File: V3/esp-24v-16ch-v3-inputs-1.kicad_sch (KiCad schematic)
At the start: 100 parts, among them U10 OR-3H4-4, U11 OR-3H4-4, U8 OR-3H4-4, U9 OR-3H4-4

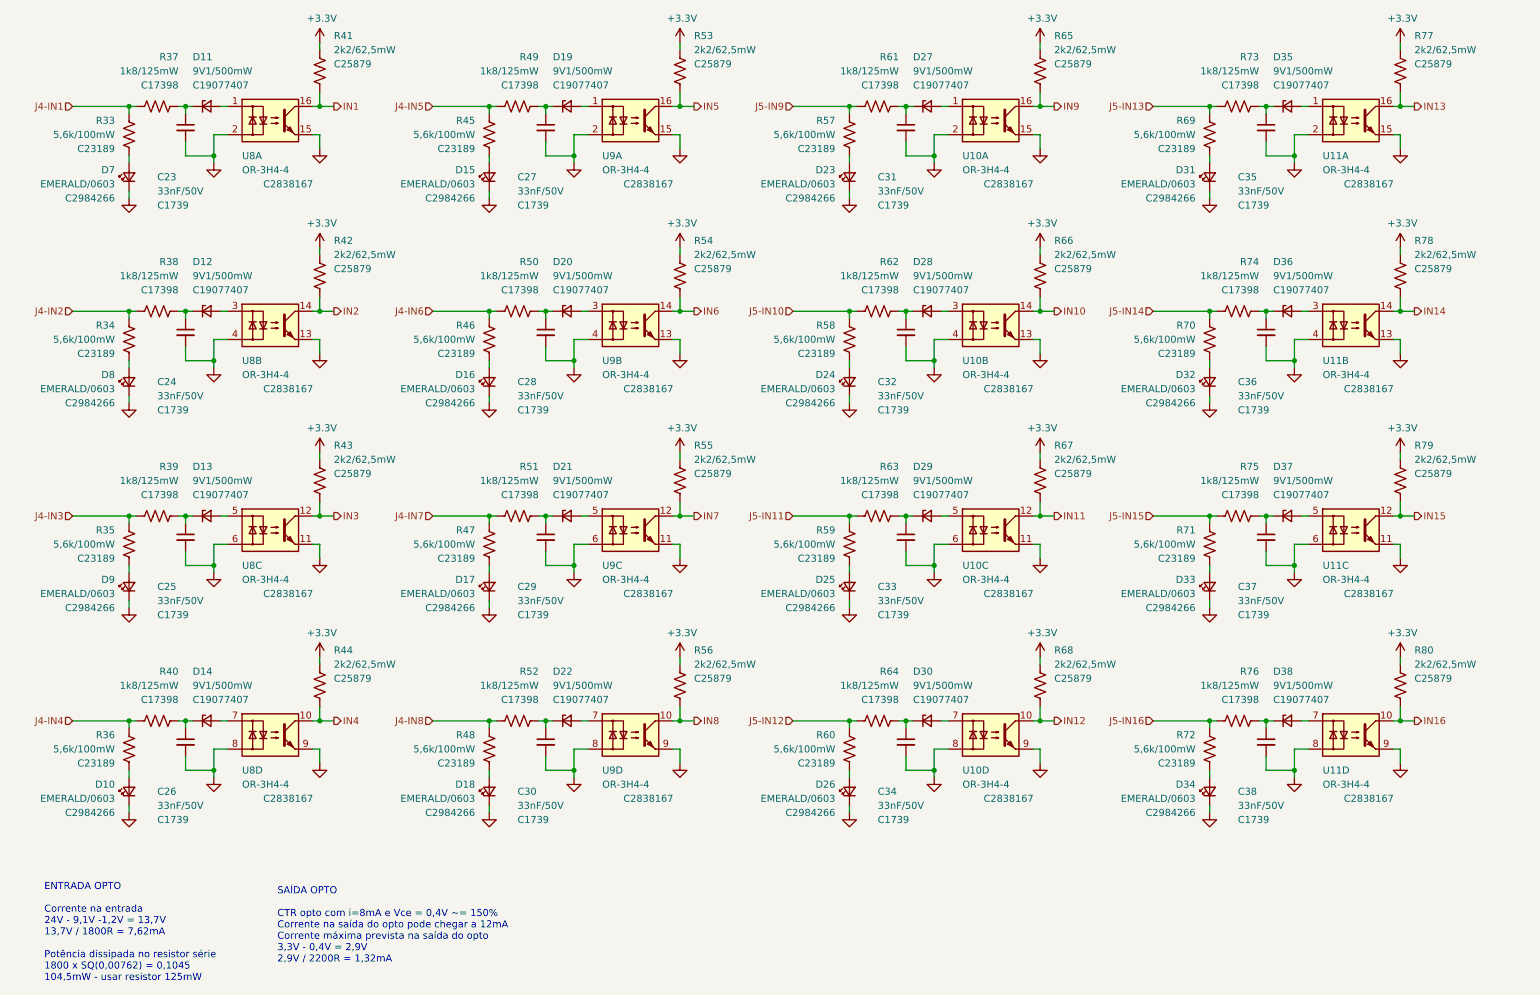
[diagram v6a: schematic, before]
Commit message: Improvements to high speed signals routing
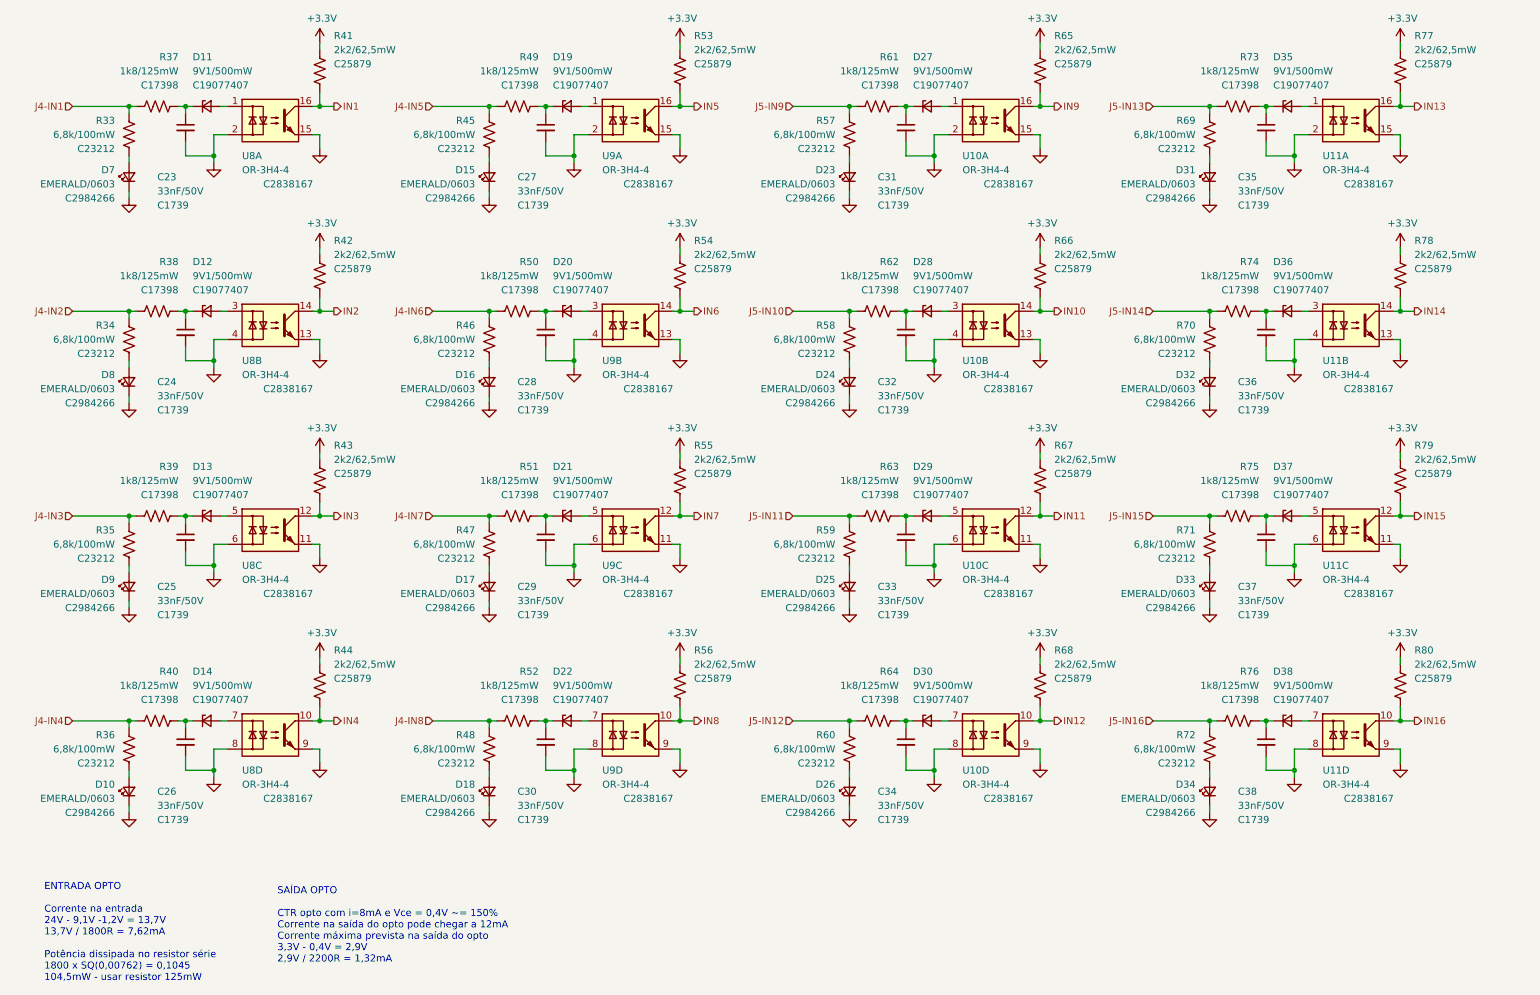
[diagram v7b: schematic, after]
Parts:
- R33, R34, R35, R36, R45, R46, R47, R48, R57, R58, R59, R60, R69, R70, R71, R72: value 5,6k/100mW -> 6,8k/100mW; LCSC Part # C23189 -> C23212; Mfr PN 0603WAF5601T5E -> 0603WAF6801T5E; Vendor PN C23189 -> C23212
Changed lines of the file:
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@@
 			)
 		)
-		(property "Value" "5,6k/100mW"
+		(property "Value" "6,8k/100mW"
 			(at 224.79 76.2 0)
 			(effects
@@
 			)
 		)
-		(property "Mfr PN" "0603WAF5601T5E"
+		(property "Mfr PN" "0603WAF6801T5E"
 			(at 227.33 76.2 0)
 			(effects
@@
 			)
 		)
-		(property "Vendor PN" "C23189"
+		(property "Vendor PN" "C23212 "
 			(at 227.33 76.2 0)
 			(effects
@@
 			)
 		)
-		(property "LCSC Part #" "C23189"
+		(property "LCSC Part #" "C23212"
 			(at 224.79 78.74 0)
 			(effects
@@
 			)
 		)
-		(property "Value" "5,6k/100mW"
+		(property "Value" "6,8k/100mW"
 			(at 95.25 113.03 0)
 			(effects
@@
 			)
 		)
-		(property "Mfr PN" "0603WAF5601T5E"
+		(property "Mfr PN" "0603WAF6801T5E"
 			(at 97.79 113.03 0)
 			(effects
@@
 			)
 		)
-		(property "Vendor PN" "C23189"
+		(property "Vendor PN" "C23212 "
 			(at 97.79 113.03 0)
 			(effects
@@
 			)
 		)
-		(property "LCSC Part #" "C23189"
+		(property "LCSC Part #" "C23212"
 			(at 95.25 115.57 0)
 			(effects
@@
 			)
 		)
-		(property "Value" "5,6k/100mW"
+		(property "Value" "6,8k/100mW"
 			(at 224.79 113.03 0)
 			(effects
@@
 			)
 		)
-		(property "Mfr PN" "0603WAF5601T5E"
+		(property "Mfr PN" "0603WAF6801T5E"
 			(at 227.33 113.03 0)
 			(effects
@@
 			)
 		)
-		(property "Vendor PN" "C23189"
+		(property "Vendor PN" "C23212 "
 			(at 227.33 113.03 0)
 			(effects
@@
 			)
 		)
-		(property "LCSC Part #" "C23189"
+		(property "LCSC Part #" "C23212"
 			(at 224.79 115.57 0)
 			(effects
@@
 			)
 		)
-		(property "Value" "5,6k/100mW"
+		(property "Value" "6,8k/100mW"
 			(at 30.48 39.37 0)
 			(effects
@@
 			)
 		)
-		(property "Mfr PN" "0603WAF5601T5E"
+		(property "Mfr PN" "0603WAF6801T5E"
 			(at 33.02 39.37 0)
 			(effects
@@
 			)
 		)
-		(property "Vendor PN" "C23189"
+		(property "Vendor PN" "C23212 "
 			(at 33.02 39.37 0)
 			(effects
@@
 			)
 		)
-		(property "LCSC Part #" "C23189"
+		(property "LCSC Part #" "C23212"
 			(at 30.48 41.91 0)
 			(effects
@@
 			)
 		)
-		(property "Value" "5,6k/100mW"
+		(property "Value" "6,8k/100mW"
 			(at 224.79 39.37 0)
 			(effects
@@
 			)
 		)
-		(property "Mfr PN" "0603WAF5601T5E"
+		(property "Mfr PN" "0603WAF6801T5E"
 			(at 227.33 39.37 0)
 			(effects
@@
 			)
 		)
-		(property "Vendor PN" "C23189"
+		(property "Vendor PN" "C23212 "
 			(at 227.33 39.37 0)
 			(effects
@@
 			)
 		)
-		(property "LCSC Part #" "C23189"
+		(property "LCSC Part #" "C23212"
 			(at 224.79 41.91 0)
 			(effects
@@
 			)
 		)
-		(property "Value" "5,6k/100mW"
+		(property "Value" "6,8k/100mW"
 			(at 30.48 113.03 0)
 			(effects
@@
 			)
 		)
-		(property "Mfr PN" "0603WAF5601T5E"
+		(property "Mfr PN" "0603WAF6801T5E"
 			(at 33.02 113.03 0)
 			(effects
@@
 			)
 		)
-		(property "Vendor PN" "C23189"
+		(property "Vendor PN" "C23212 "
 			(at 33.02 113.03 0)
 			(effects
@@
 			)
 		)
-		(property "LCSC Part #" "C23189"
+		(property "LCSC Part #" "C23212"
 			(at 30.48 115.57 0)
 			(effects
@@
 			)
 		)
-		(property "Value" "5,6k/100mW"
+		(property "Value" "6,8k/100mW"
 			(at 95.25 39.37 0)
 			(effects
@@
 			)
 		)
-		(property "Mfr PN" "0603WAF5601T5E"
+		(property "Mfr PN" "0603WAF6801T5E"
 			(at 97.79 39.37 0)
 			(effects
@@
 			)
 		)
-		(property "Vendor PN" "C23189"
+		(property "Vendor PN" "C23212 "
 			(at 97.79 39.37 0)
 			(effects
@@
 			)
 		)
-		(property "LCSC Part #" "C23189"
+		(property "LCSC Part #" "C23212"
 			(at 95.25 41.91 0)
 			(effects
@@
 			)
 		)
-		(property "Value" "5,6k/100mW"
+		(property "Value" "6,8k/100mW"
 			(at 95.25 149.86 0)
 			(effects
@@
 			)
 		)
-		(property "Mfr PN" "0603WAF5601T5E"
+		(property "Mfr PN" "0603WAF6801T5E"
 			(at 97.79 149.86 0)
 			(effects
@@
 			)
 		)
-		(property "Vendor PN" "C23189"
+		(property "Vendor PN" "C23212 "
 			(at 97.79 149.86 0)
 			(effects
@@
 			)
 		)
-		(property "LCSC Part #" "C23189"
+		(property "LCSC Part #" "C23212"
 			(at 95.25 152.4 0)
 			(effects
@@
 			)
 		)
-		(property "Value" "5,6k/100mW"
+		(property "Value" "6,8k/100mW"
 			(at 160.02 149.86 0)
 			(effects
@@
 			)
 		)
-		(property "Mfr PN" "0603WAF5601T5E"
+		(property "Mfr PN" "0603WAF6801T5E"
 			(at 162.56 149.86 0)
 			(effects
@@
 			)
 		)
-		(property "Vendor PN" "C23189"
+		(property "Vendor PN" "C23212 "
 			(at 162.56 149.86 0)
 			(effects
@@
 			)
 		)
-		(property "LCSC Part #" "C23189"
+		(property "LCSC Part #" "C23212"
 			(at 160.02 152.4 0)
 			(effects
@@
 			)
 		)
-		(property "Value" "5,6k/100mW"
+		(property "Value" "6,8k/100mW"
 			(at 95.25 76.2 0)
 			(effects
@@
 			)
 		)
-		(property "Mfr PN" "0603WAF5601T5E"
+		(property "Mfr PN" "0603WAF6801T5E"
 			(at 97.79 76.2 0)
 			(effects
@@
 			)
 		)
-		(property "Vendor PN" "C23189"
+		(property "Vendor PN" "C23212 "
 			(at 97.79 76.2 0)
 			(effects
@@
 			)
 		)
-		(property "LCSC Part #" "C23189"
+		(property "LCSC Part #" "C23212"
 			(at 95.25 78.74 0)
 			(effects
@@
 			)
 		)
-		(property "Value" "5,6k/100mW"
+		(property "Value" "6,8k/100mW"
 			(at 160.02 76.2 0)
 			(effects
@@
 			)
 		)
-		(property "Mfr PN" "0603WAF5601T5E"
+		(property "Mfr PN" "0603WAF6801T5E"
 			(at 162.56 76.2 0)
 			(effects
@@
 			)
 		)
-		(property "Vendor PN" "C23189"
+		(property "Vendor PN" "C23212 "
 			(at 162.56 76.2 0)
 			(effects
@@
 			)
 		)
-		(property "LCSC Part #" "C23189"
+		(property "LCSC Part #" "C23212"
 			(at 160.02 78.74 0)
 			(effects
@@
 			)
 		)
-		(property "Value" "5,6k/100mW"
+		(property "Value" "6,8k/100mW"
 			(at 224.79 149.86 0)
 			(effects
@@
 			)
 		)
-		(property "Mfr PN" "0603WAF5601T5E"
+		(property "Mfr PN" "0603WAF6801T5E"
 			(at 227.33 149.86 0)
 			(effects
@@
 			)
 		)
-		(property "Vendor PN" "C23189"
+		(property "Vendor PN" "C23212 "
 			(at 227.33 149.86 0)
 			(effects
@@
 			)
 		)
-		(property "LCSC Part #" "C23189"
+		(property "LCSC Part #" "C23212"
 			(at 224.79 152.4 0)
 			(effects
@@
 			)
 		)
-		(property "Value" "5,6k/100mW"
+		(property "Value" "6,8k/100mW"
 			(at 30.48 76.2 0)
 			(effects
@@
 			)
 		)
-		(property "Mfr PN" "0603WAF5601T5E"
+		(property "Mfr PN" "0603WAF6801T5E"
 			(at 33.02 76.2 0)
 			(effects
@@
 			)
 		)
-		(property "Vendor PN" "C23189"
+		(property "Vendor PN" "C23212 "
 			(at 33.02 76.2 0)
 			(effects
@@
 			)
 		)
-		(property "LCSC Part #" "C23189"
+		(property "LCSC Part #" "C23212"
 			(at 30.48 78.74 0)
 			(effects
@@
 			)
 		)
-		(property "Value" "5,6k/100mW"
+		(property "Value" "6,8k/100mW"
 			(at 160.02 39.37 0)
 			(effects
@@
 			)
 		)
-		(property "Mfr PN" "0603WAF5601T5E"
+		(property "Mfr PN" "0603WAF6801T5E"
 			(at 162.56 39.37 0)
 			(effects
@@
 			)
 		)
-		(property "Vendor PN" "C23189"
+		(property "Vendor PN" "C23212 "
 			(at 162.56 39.37 0)
 			(effects
@@
 			)
 		)
-		(property "LCSC Part #" "C23189"
+		(property "LCSC Part #" "C23212"
 			(at 160.02 41.91 0)
 			(effects
@@
 			)
 		)
-		(property "Value" "5,6k/100mW"
+		(property "Value" "6,8k/100mW"
 			(at 160.02 113.03 0)
 			(effects
@@
 			)
 		)
-		(property "Mfr PN" "0603WAF5601T5E"
+		(property "Mfr PN" "0603WAF6801T5E"
 			(at 162.56 113.03 0)
 			(effects
@@
 			)
 		)
-		(property "Vendor PN" "C23189"
+		(property "Vendor PN" "C23212 "
 			(at 162.56 113.03 0)
 			(effects
@@
 			)
 		)
-		(property "LCSC Part #" "C23189"
+		(property "LCSC Part #" "C23212"
 			(at 160.02 115.57 0)
 			(effects
@@
 			)
 		)
-		(property "Value" "5,6k/100mW"
+		(property "Value" "6,8k/100mW"
 			(at 30.48 149.86 0)
 			(effects
@@
 			)
 		)
-		(property "Mfr PN" "0603WAF5601T5E"
+		(property "Mfr PN" "0603WAF6801T5E"
 			(at 33.02 149.86 0)
 			(effects
@@
 			)
 		)
-		(property "Vendor PN" "C23189"
+		(property "Vendor PN" "C23212 "
 			(at 33.02 149.86 0)
 			(effects
@@
 			)
 		)
-		(property "LCSC Part #" "C23189"
+		(property "LCSC Part #" "C23212"
 			(at 30.48 152.4 0)
 			(effects

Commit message: Renamed to V3.2
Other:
- title: ESP 16x 24VDC Input 16x 24VDC Output Module -> ESP 24V 16xIn/16xOut/4xNTC Module
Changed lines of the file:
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@@
 	(paper "A4")
 	(title_block
-		(title "ESP 16x 24VDC Input 16x 24VDC Output Module")
-		(date "2024-11-06")
-		(rev "V3")
+		(title "ESP 24V 16xIn/16xOut/4xNTC Module")
+		(date "2025-06-29")
+		(rev "V3.2")
 	)
 	(junction
